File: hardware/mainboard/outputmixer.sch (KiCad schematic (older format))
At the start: 13 parts, among them U15 TL072

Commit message: First pass layout & component selection for mainboard
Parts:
- C44, C45: footprint Capacitor_SMD:C_0805_2012Metric_Pad1.15x1.40mm_HandSolder -> Capacitor_SMD:C_0603_1608Metric_Pad1.05x0.95mm_HandSolder; finalized (none) -> yes; mpn (none) -> MF-CAP-0603-18pF
- C46, C47: footprint Capacitor_SMD:C_0805_2012Metric_Pad1.15x1.40mm_HandSolder -> Capacitor_SMD:C_0603_1608Metric_Pad1.05x0.95mm_HandSolder; finalized (none) -> yes; mpn (none) -> MF-CAP-0603-0.1uF
- R63, R64, R65, R66, R67, R68, R69, R70: footprint Resistor_SMD:R_1206_3216Metric_Pad1.42x1.75mm_HandSolder -> Resistor_SMD:R_0603_1608Metric_Pad1.05x0.95mm_HandSolder; Reqs (none) -> 0.5%; finalized (none) -> yes; mpn (none) -> ERA-3AED104V
- U15: finalized (none) -> yes; mpn (none) -> TL072CPWR
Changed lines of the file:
@@
 $Descr USLetter 11000 8500
 encoding utf-8
-Sheet 5 7
+Sheet 3 7
 Title ""
 Date ""
@@
 F 2 "Package_SO:TSSOP-8_4.4x3mm_P0.65mm" H 3400 4150 50  0001 C CNN
 F 3 "http://www.ti.com/lit/ds/symlink/tl071.pdf" H 3400 4150 50  0001 C CNN
+F 4 "yes" H 3400 4150 50  0001 C CNN "finalized"
+F 5 "TL072CPWR" H 3400 4150 50  0001 C CNN "mpn"
 	2    3400 4150
 	1    0    0    1
@@
 F 2 "Package_SO:TSSOP-8_4.4x3mm_P0.65mm" H 6100 3050 50  0001 C CNN
 F 3 "http://www.ti.com/lit/ds/symlink/tl071.pdf" H 6100 3050 50  0001 C CNN
+F 4 "yes" H 6100 3050 50  0001 C CNN "finalized"
+F 5 "TL072CPWR" H 6100 3050 50  0001 C CNN "mpn"
 	3    6100 3050
 	1    0    0    -1
@@
 F 0 "R65" V 2595 2300 50  0000 C CNN
 F 1 "100k" V 2686 2300 50  0000 C CNN
-F 2 "Resistor_SMD:R_1206_3216Metric_Pad1.42x1.75mm_HandSolder" V 2840 2290 50  0001 C CNN
+F 2 "Resistor_SMD:R_0603_1608Metric_Pad1.05x0.95mm_HandSolder" V 2840 2290 50  0001 C CNN
 F 3 "~" H 2800 2300 50  0001 C CNN
+F 4 "0.5%" H 2800 2300 50  0001 C CNN "Reqs"
+F 5 "yes" H 2800 2300 50  0001 C CNN "finalized"
+F 6 "ERA-3AED104V" H 2800 2300 50  0001 C CNN "mpn"
 	1    2800 2300
 	0    1    1    0
@@
 F 0 "R66" V 2900 2500 50  0000 C CNN
 F 1 "100k" V 3000 2500 50  0000 C CNN
-F 2 "Resistor_SMD:R_1206_3216Metric_Pad1.42x1.75mm_HandSolder" V 2840 2490 50  0001 C CNN
+F 2 "Resistor_SMD:R_0603_1608Metric_Pad1.05x0.95mm_HandSolder" V 2840 2490 50  0001 C CNN
 F 3 "~" H 2800 2500 50  0001 C CNN
+F 4 "0.5%" H 2800 2500 50  0001 C CNN "Reqs"
+F 5 "yes" H 2800 2500 50  0001 C CNN "finalized"
+F 6 "ERA-3AED104V" H 2800 2500 50  0001 C CNN "mpn"
 	1    2800 2500
 	0    1    1    0
@@
 F 0 "R67" H 3032 2754 50  0000 R CNN
 F 1 "100k" H 3032 2845 50  0000 R CNN
-F 2 "Resistor_SMD:R_1206_3216Metric_Pad1.42x1.75mm_HandSolder" V 3140 2790 50  0001 C CNN
+F 2 "Resistor_SMD:R_0603_1608Metric_Pad1.05x0.95mm_HandSolder" V 3140 2790 50  0001 C CNN
 F 3 "~" H 3100 2800 50  0001 C CNN
+F 4 "0.5%" H 3100 2800 50  0001 C CNN "Reqs"
+F 5 "yes" H 3100 2800 50  0001 C CNN "finalized"
+F 6 "ERA-3AED104V" H 3100 2800 50  0001 C CNN "mpn"
 	1    3100 2800
 	-1   0    0    1
@@
 F 2 "Package_SO:TSSOP-8_4.4x3mm_P0.65mm" H 3400 2400 50  0001 C CNN
 F 3 "http://www.ti.com/lit/ds/symlink/tl071.pdf" H 3400 2400 50  0001 C CNN
+F 4 "yes" H 3400 2400 50  0001 C CNN "finalized"
+F 5 "TL072CPWR" H 3400 2400 50  0001 C CNN "mpn"
 	1    3400 2400
 	1    0    0    1
@@
 F 0 "R68" V 3555 2050 50  0000 C CNN
 F 1 "100k" V 3464 2050 50  0000 C CNN
-F 2 "Resistor_SMD:R_1206_3216Metric_Pad1.42x1.75mm_HandSolder" V 3390 2040 50  0001 C CNN
+F 2 "Resistor_SMD:R_0603_1608Metric_Pad1.05x0.95mm_HandSolder" V 3390 2040 50  0001 C CNN
 F 3 "~" H 3350 2050 50  0001 C CNN
+F 4 "0.5%" H 3350 2050 50  0001 C CNN "Reqs"
+F 5 "yes" H 3350 2050 50  0001 C CNN "finalized"
+F 6 "ERA-3AED104V" H 3350 2050 50  0001 C CNN "mpn"
 	1    3350 2050
 	0    -1   -1   0
@@
 F 0 "R63" V 2750 3700 50  0000 L CNN
 F 1 "100k" V 2550 3650 50  0000 L CNN
-F 2 "Resistor_SMD:R_1206_3216Metric_Pad1.42x1.75mm_HandSolder" V 2690 3740 50  0001 C CNN
+F 2 "Resistor_SMD:R_0603_1608Metric_Pad1.05x0.95mm_HandSolder" V 2690 3740 50  0001 C CNN
 F 3 "~" H 2650 3750 50  0001 C CNN
+F 4 "0.5%" H 2650 3750 50  0001 C CNN "Reqs"
+F 5 "yes" H 2650 3750 50  0001 C CNN "finalized"
+F 6 "ERA-3AED104V" H 2650 3750 50  0001 C CNN "mpn"
 	1    2650 3750
 	0    -1   -1   0
@@
 F 0 "C44" V 3121 1700 50  0000 C CNN
 F 1 "18pF" V 3212 1700 50  0000 C CNN
-F 2 "Capacitor_SMD:C_0805_2012Metric_Pad1.15x1.40mm_HandSolder" H 3350 1700 50  0001 C CNN
+F 2 "Capacitor_SMD:C_0603_1608Metric_Pad1.05x0.95mm_HandSolder" H 3350 1700 50  0001 C CNN
 F 3 "~" H 3350 1700 50  0001 C CNN
+F 4 "yes" H 3350 1700 50  0001 C CNN "finalized"
+F 5 "MF-CAP-0603-18pF" H 3350 1700 50  0001 C CNN "mpn"
 	1    3350 1700
 	0    1    1    0
@@
 F 0 "R64" V 2750 4000 50  0000 L CNN
 F 1 "100k" V 2550 3950 50  0000 L CNN
-F 2 "Resistor_SMD:R_1206_3216Metric_Pad1.42x1.75mm_HandSolder" V 2690 4040 50  0001 C CNN
+F 2 "Resistor_SMD:R_0603_1608Metric_Pad1.05x0.95mm_HandSolder" V 2690 4040 50  0001 C CNN
 F 3 "~" H 2650 4050 50  0001 C CNN
+F 4 "0.5%" H 2650 4050 50  0001 C CNN "Reqs"
+F 5 "yes" H 2650 4050 50  0001 C CNN "finalized"
+F 6 "ERA-3AED104V" H 2650 4050 50  0001 C CNN "mpn"
 	1    2650 4050
 	0    -1   -1   0
@@
 F 0 "R69" V 3605 3800 50  0000 C CNN
 F 1 "100k" V 3514 3800 50  0000 C CNN
-F 2 "Resistor_SMD:R_1206_3216Metric_Pad1.42x1.75mm_HandSolder" V 3440 3790 50  0001 C CNN
+F 2 "Resistor_SMD:R_0603_1608Metric_Pad1.05x0.95mm_HandSolder" V 3440 3790 50  0001 C CNN
 F 3 "~" H 3400 3800 50  0001 C CNN
+F 4 "0.5%" H 3400 3800 50  0001 C CNN "Reqs"
+F 5 "yes" H 3400 3800 50  0001 C CNN "finalized"
+F 6 "ERA-3AED104V" H 3400 3800 50  0001 C CNN "mpn"
 	1    3400 3800
 	0    -1   -1   0
@@
 F 0 "R70" V 4205 4150 50  0000 C CNN
 F 1 "100k" V 4114 4150 50  0000 C CNN
-F 2 "Resistor_SMD:R_1206_3216Metric_Pad1.42x1.75mm_HandSolder" V 4040 4140 50  0001 C CNN
+F 2 "Resistor_SMD:R_0603_1608Metric_Pad1.05x0.95mm_HandSolder" V 4040 4140 50  0001 C CNN
 F 3 "~" H 4000 4150 50  0001 C CNN
+F 4 "0.5%" H 4000 4150 50  0001 C CNN "Reqs"
+F 5 "yes" H 4000 4150 50  0001 C CNN "finalized"
+F 6 "ERA-3AED104V" H 4000 4150 50  0001 C CNN "mpn"
 	1    4000 4150
 	0    -1   -1   0
@@
 F 0 "C45" V 3171 3450 50  0000 C CNN
 F 1 "18pF" V 3262 3450 50  0000 C CNN
-F 2 "Capacitor_SMD:C_0805_2012Metric_Pad1.15x1.40mm_HandSolder" H 3400 3450 50  0001 C CNN
+F 2 "Capacitor_SMD:C_0603_1608Metric_Pad1.05x0.95mm_HandSolder" H 3400 3450 50  0001 C CNN
 F 3 "~" H 3400 3450 50  0001 C CNN
+F 4 "yes" H 3400 3450 50  0001 C CNN "finalized"
+F 5 "MF-CAP-0603-18pF" H 3400 3450 50  0001 C CNN "mpn"
 	1    3400 3450
 	0    1    1    0
@@
 F 0 "C46" H 6508 3054 50  0000 R CNN
 F 1 "0.1uF" H 6508 3145 50  0000 R CNN
-F 2 "Capacitor_SMD:C_0805_2012Metric_Pad1.15x1.40mm_HandSolder" H 6600 3100 50  0001 C CNN
+F 2 "Capacitor_SMD:C_0603_1608Metric_Pad1.05x0.95mm_HandSolder" H 6600 3100 50  0001 C CNN
 F 3 "~" H 6600 3100 50  0001 C CNN
+F 4 "yes" H 6600 3100 50  0001 C CNN "finalized"
+F 5 "MF-CAP-0603-0.1uF" H 6600 3100 50  0001 C CNN "mpn"
 	1    6600 3100
 	-1   0    0    1
@@
 F 0 "C47" H 7008 3054 50  0000 R CNN
 F 1 "0.1uF" H 7008 3145 50  0000 R CNN
-F 2 "Capacitor_SMD:C_0805_2012Metric_Pad1.15x1.40mm_HandSolder" H 7100 3100 50  0001 C CNN
+F 2 "Capacitor_SMD:C_0603_1608Metric_Pad1.05x0.95mm_HandSolder" H 7100 3100 50  0001 C CNN
 F 3 "~" H 7100 3100 50  0001 C CNN
+F 4 "yes" H 7100 3100 50  0001 C CNN "finalized"
+F 5 "MF-CAP-0603-0.1uF" H 7100 3100 50  0001 C CNN "mpn"
 	1    7100 3100
 	-1   0    0    1

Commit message: Check passive ratings
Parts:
- C44, C45: mpn specs (none) -> 5% 50v
- C46, C47: mpn specs (none) -> 10%, 25v
- R63, R64, R65, R66, R67, R68, R69, R70: mpn specs (none) -> 100mW
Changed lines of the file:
@@
 F 5 "yes" H 2800 2300 50  0001 C CNN "finalized"
 F 6 "ERA-3AED104V" H 2800 2300 50  0001 C CNN "mpn"
+F 7 "100mW" H 2800 2300 50  0001 C CNN "mpn specs"
 	1    2800 2300
 	0    1    1    0
@@
 F 5 "yes" H 2800 2500 50  0001 C CNN "finalized"
 F 6 "ERA-3AED104V" H 2800 2500 50  0001 C CNN "mpn"
+F 7 "100mW" H 2800 2500 50  0001 C CNN "mpn specs"
 	1    2800 2500
 	0    1    1    0
@@
 F 5 "yes" H 3100 2800 50  0001 C CNN "finalized"
 F 6 "ERA-3AED104V" H 3100 2800 50  0001 C CNN "mpn"
+F 7 "100mW" H 3100 2800 50  0001 C CNN "mpn specs"
 	1    3100 2800
 	-1   0    0    1
@@
 F 5 "yes" H 3350 2050 50  0001 C CNN "finalized"
 F 6 "ERA-3AED104V" H 3350 2050 50  0001 C CNN "mpn"
+F 7 "100mW" H 3350 2050 50  0001 C CNN "mpn specs"
 	1    3350 2050
 	0    -1   -1   0
@@
 F 5 "yes" H 2650 3750 50  0001 C CNN "finalized"
 F 6 "ERA-3AED104V" H 2650 3750 50  0001 C CNN "mpn"
+F 7 "100mW" H 2650 3750 50  0001 C CNN "mpn specs"
 	1    2650 3750
 	0    -1   -1   0
@@
 F 4 "yes" H 3350 1700 50  0001 C CNN "finalized"
 F 5 "MF-CAP-0603-18pF" H 3350 1700 50  0001 C CNN "mpn"
+F 6 "5% 50v" H 3350 1700 50  0001 C CNN "mpn specs"
 	1    3350 1700
 	0    1    1    0
@@
 F 5 "yes" H 2650 4050 50  0001 C CNN "finalized"
 F 6 "ERA-3AED104V" H 2650 4050 50  0001 C CNN "mpn"
+F 7 "100mW" H 2650 4050 50  0001 C CNN "mpn specs"
 	1    2650 4050
 	0    -1   -1   0
@@
 F 5 "yes" H 3400 3800 50  0001 C CNN "finalized"
 F 6 "ERA-3AED104V" H 3400 3800 50  0001 C CNN "mpn"
+F 7 "100mW" H 3400 3800 50  0001 C CNN "mpn specs"
 	1    3400 3800
 	0    -1   -1   0
@@
 F 5 "yes" H 4000 4150 50  0001 C CNN "finalized"
 F 6 "ERA-3AED104V" H 4000 4150 50  0001 C CNN "mpn"
+F 7 "100mW" H 4000 4150 50  0001 C CNN "mpn specs"
 	1    4000 4150
 	0    -1   -1   0
@@
 F 4 "yes" H 3400 3450 50  0001 C CNN "finalized"
 F 5 "MF-CAP-0603-18pF" H 3400 3450 50  0001 C CNN "mpn"
+F 6 "5% 50v" H 3400 3450 50  0001 C CNN "mpn specs"
 	1    3400 3450
 	0    1    1    0
@@
 F 4 "yes" H 6600 3100 50  0001 C CNN "finalized"
 F 5 "MF-CAP-0603-0.1uF" H 6600 3100 50  0001 C CNN "mpn"
+F 6 "10%, 25v" H 6600 3100 50  0001 C CNN "mpn specs"
 	1    6600 3100
 	-1   0    0    1
@@
 F 4 "yes" H 7100 3100 50  0001 C CNN "finalized"
 F 5 "MF-CAP-0603-0.1uF" H 7100 3100 50  0001 C CNN "mpn"
+F 6 "10%, 25v" H 7100 3100 50  0001 C CNN "mpn specs"
 	1    7100 3100
 	-1   0    0    1

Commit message: Bumb schematics after generating gerbers and assigning alt mpns
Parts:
- C44, C45: mpn alt (none) -> GCM1885C2A180JA16D
- C46, C47: mpn alt (none) -> GRM188R72A104KA35D
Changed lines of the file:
@@
 F 5 "MF-CAP-0603-18pF" H 3350 1700 50  0001 C CNN "mpn"
 F 6 "5% 50v" H 3350 1700 50  0001 C CNN "mpn specs"
+F 7 "GCM1885C2A180JA16D" H 3350 1700 50  0001 C CNN "mpn alt"
 	1    3350 1700
 	0    1    1    0
@@
 F 5 "MF-CAP-0603-18pF" H 3400 3450 50  0001 C CNN "mpn"
 F 6 "5% 50v" H 3400 3450 50  0001 C CNN "mpn specs"
+F 7 "GCM1885C2A180JA16D" H 3400 3450 50  0001 C CNN "mpn alt"
 	1    3400 3450
 	0    1    1    0
@@
 F 5 "MF-CAP-0603-0.1uF" H 6600 3100 50  0001 C CNN "mpn"
 F 6 "10%, 25v" H 6600 3100 50  0001 C CNN "mpn specs"
+F 7 "GRM188R72A104KA35D" H 6600 3100 50  0001 C CNN "mpn alt"
 	1    6600 3100
 	-1   0    0    1
@@
 F 5 "MF-CAP-0603-0.1uF" H 7100 3100 50  0001 C CNN "mpn"
 F 6 "10%, 25v" H 7100 3100 50  0001 C CNN "mpn specs"
+F 7 "GRM188R72A104KA35D" H 7100 3100 50  0001 C CNN "mpn alt"
 	1    7100 3100
 	-1   0    0    1

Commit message: Fix a few more mpns
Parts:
- C46, C47: mpn alt GRM188R72A104KA35D -> GCM188R91E104KA37D
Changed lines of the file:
@@
 F 5 "MF-CAP-0603-0.1uF" H 6600 3100 50  0001 C CNN "mpn"
 F 6 "10%, 25v" H 6600 3100 50  0001 C CNN "mpn specs"
-F 7 "GRM188R72A104KA35D" H 6600 3100 50  0001 C CNN "mpn alt"
+F 7 "GCM188R91E104KA37D" H 6600 3100 50  0001 C CNN "mpn alt"
 	1    6600 3100
 	-1   0    0    1
@@
 F 5 "MF-CAP-0603-0.1uF" H 7100 3100 50  0001 C CNN "mpn"
 F 6 "10%, 25v" H 7100 3100 50  0001 C CNN "mpn specs"
-F 7 "GRM188R72A104KA35D" H 7100 3100 50  0001 C CNN "mpn alt"
+F 7 "GCM188R91E104KA37D" H 7100 3100 50  0001 C CNN "mpn alt"
 	1    7100 3100
 	-1   0    0    1

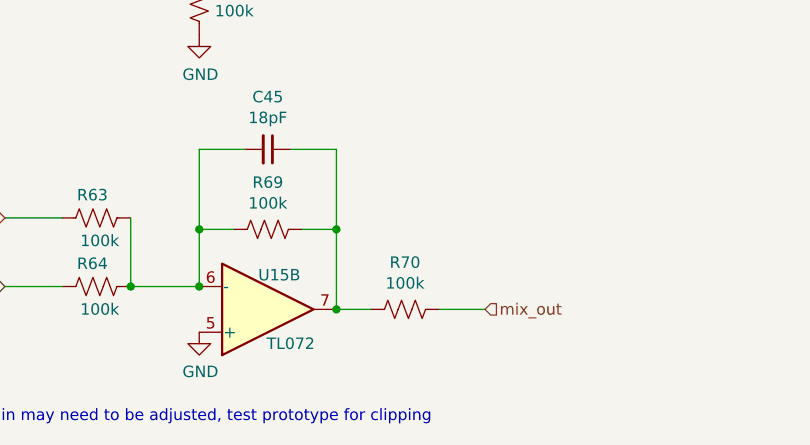
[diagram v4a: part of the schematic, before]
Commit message: Change R70 from 100k to 1k
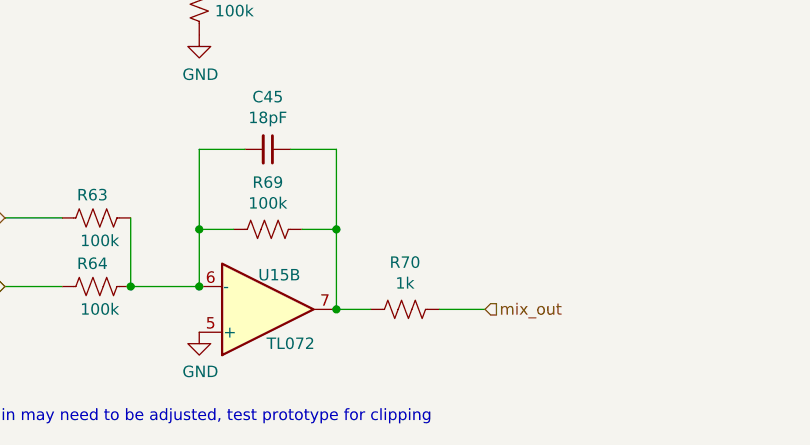
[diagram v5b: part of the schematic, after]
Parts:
- R70: value 100k -> 1k; mpn ERA-3AED104V -> ERA-3AED102V
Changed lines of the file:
@@
 P 4000 4150
 F 0 "R70" V 4205 4150 50  0000 C CNN
-F 1 "100k" V 4114 4150 50  0000 C CNN
+F 1 "1k" V 4114 4150 50  0000 C CNN
 F 2 "Resistor_SMD:R_0603_1608Metric_Pad1.05x0.95mm_HandSolder" V 4040 4140 50  0001 C CNN
 F 3 "~" H 4000 4150 50  0001 C CNN
 F 4 "0.5%" H 4000 4150 50  0001 C CNN "Reqs"
 F 5 "yes" H 4000 4150 50  0001 C CNN "finalized"
-F 6 "ERA-3AED104V" H 4000 4150 50  0001 C CNN "mpn"
+F 6 "ERA-3AED102V" H 4000 4150 50  0001 C CNN "mpn"
 F 7 "100mW" H 4000 4150 50  0001 C CNN "mpn specs"
 	1    4000 4150
